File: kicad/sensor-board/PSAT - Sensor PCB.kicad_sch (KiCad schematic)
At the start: 42 parts, among them J1 533980471, J2 533980471, J3 533980471, J4 533980471, Q1 2N2222A, U1 ESP32-CAM, U2 CD-PA1616D, U3 BME280, U4 BMI323

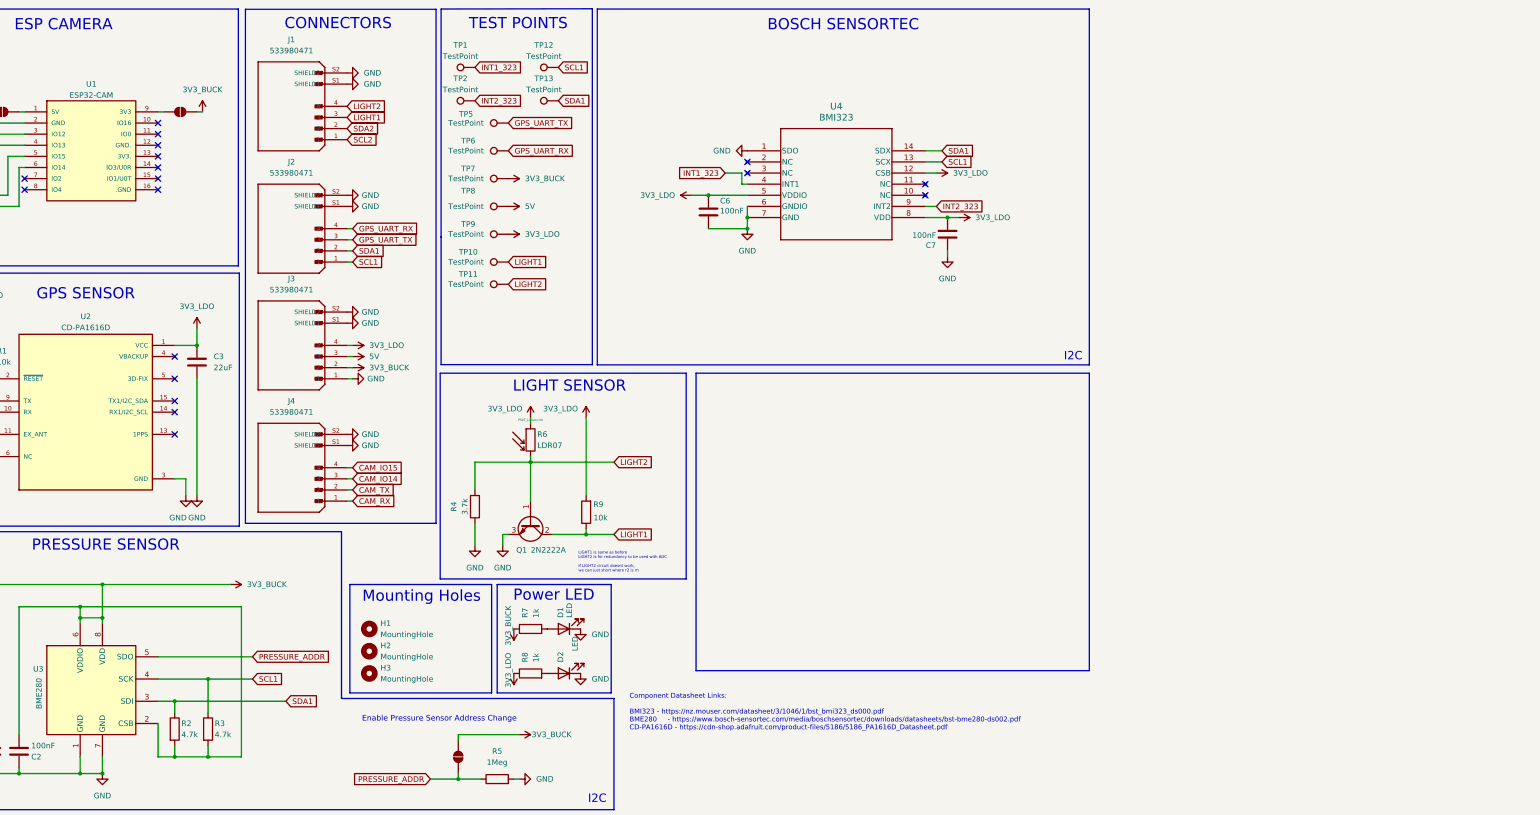
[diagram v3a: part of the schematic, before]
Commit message: feat: sensor board pcb wiring, silkscreen incomplete
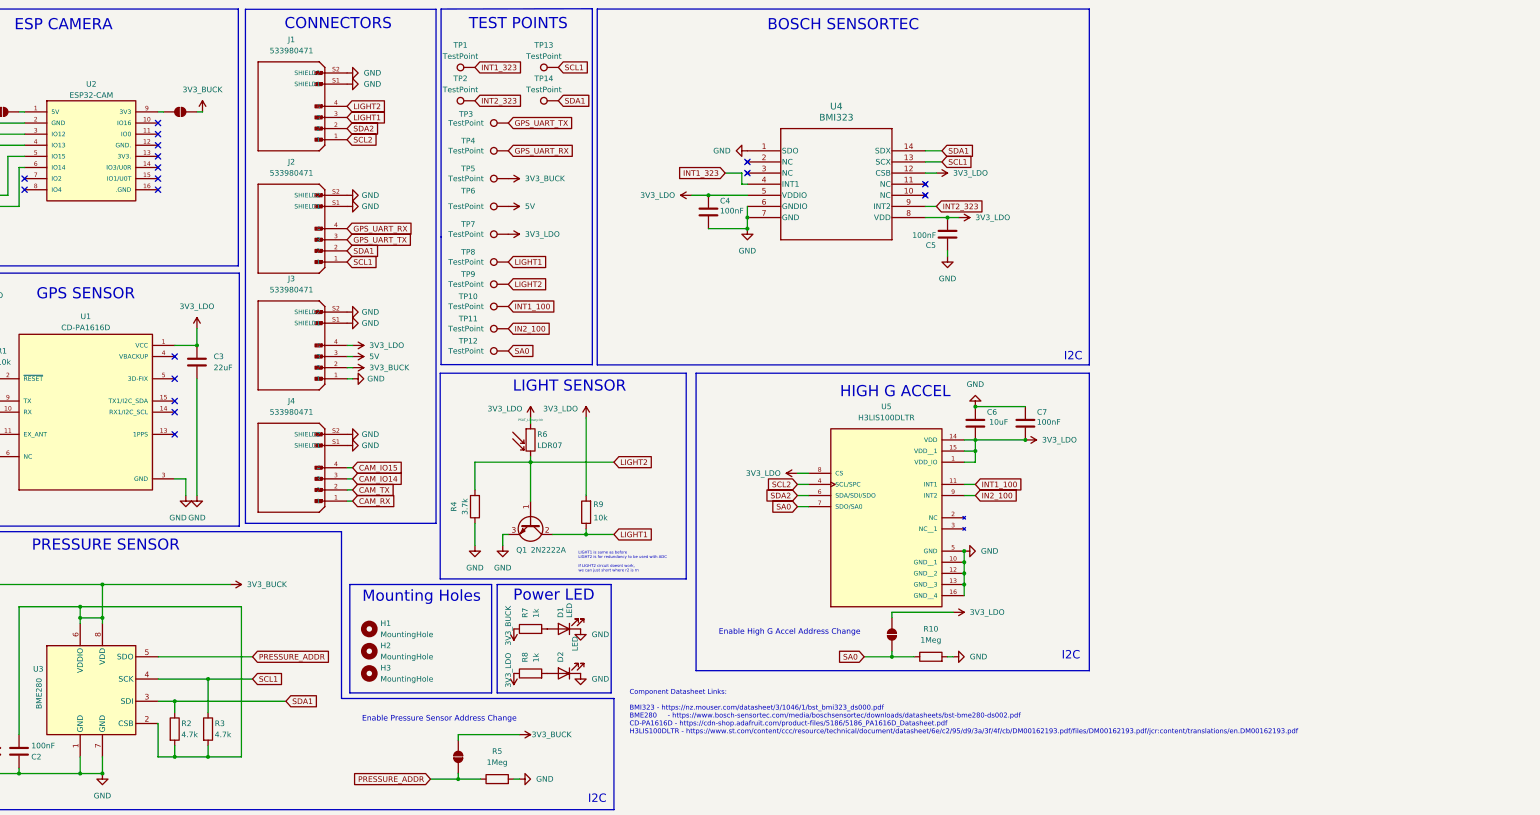
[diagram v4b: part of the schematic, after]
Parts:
- added C6: 10uF, Capacitor_SMD:C_0805_2012Metric_Pad1.18x1.45mm_HandSolder, symbol Device:C
- added C7: 100nF, Capacitor_SMD:C_0805_2012Metric_Pad1.18x1.45mm_HandSolder, symbol Device:C
- added JP4: EN_5, Jumper:SolderJumper-2_P1.3mm_Open_Pad1.0x1.5mm, symbol Jumper:SolderJumper_2_Open
- added R10: 1Meg, Resistor_SMD:R_0805_2012Metric_Pad1.20x1.40mm_HandSolder, symbol Device:R
- added TP10, TP11, TP12: TestPoint, TestPoint:TestPoint_Pad_D1.0mm, symbol Connector:TestPoint
- added U5: H3LIS100DLTR, PSAT_Library:PQFN50P300X300X100-16N, symbol H3LIS100DLTR:H3LIS100DLTR
- renumbered C6 to C4, C7 to C5, TP12 to TP13, TP13 to TP14, TP5 to TP3, TP6 to TP4, TP7 to TP5, TP8 to TP6, TP9 to TP7, TP10 to TP8, TP11 to TP9, U2 to U1, U1 to U2
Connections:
- net 3V3_LDO: now also C6.1, C7.1, JP4.1 (A), U5.1 (VDD_IO), U5.14 (VDD), U5.15 (VDD__1), U5.8 (CS)
- net GND: now also C6.2, C7.2, R10.2, U5.10 (GND__1), U5.12 (GND__2), U5.13 (GND__3), U5.16 (GND__4), U5.5 (GND)
- net SCL2: now also U5.4 (SCL/SPC)
- net SDA2: now also U5.6 (SDA/SDI/SDO)
- new net IN2_100: TP11.1, U5.9 (INT2)
- new net INT1_100: TP10.1, U5.11 (INT1)
- new net SA0: JP4.2 (B), R10.1, TP12.1, U5.7 (SDO/SA0)
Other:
- note added: "Component Datasheet Links: BMI323 - https://nz.mouser.com/datasheet/3/1046/1/bst_bmi323_ds000.pdf BME280 - https://www.bosch-sensortec.com/media/boschsensortec/downloads/datasheets/bst-bme280-ds002.pdf CD-PA1616D - https://cdn-shop.adafruit.com/product-files/5186/5186_PA1616D_Datasheet.pdf H3LIS100DLTR - https://www.st.com/content/ccc/resource/technical/document/datasheet/6e/c2/95/d9/3a/3f/4f/cb/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"
- note added: "Enable High G Accel Address Change"
- note added: "HIGH G ACCEL"
- note removed: "Component Datasheet Links: BMI323 - https://nz.mouser.com/datasheet/3/1046/1/bst_bmi323_ds000.pdf BME280 - https://www.bosch-sensortec.com/media/boschsensortec/downloads/datasheets/bst-bme280-ds002.pdf CD-PA1616D - https://cdn-shop.adafruit.com/product-files/5186/5186_PA1616D_Datasheet.pdf"

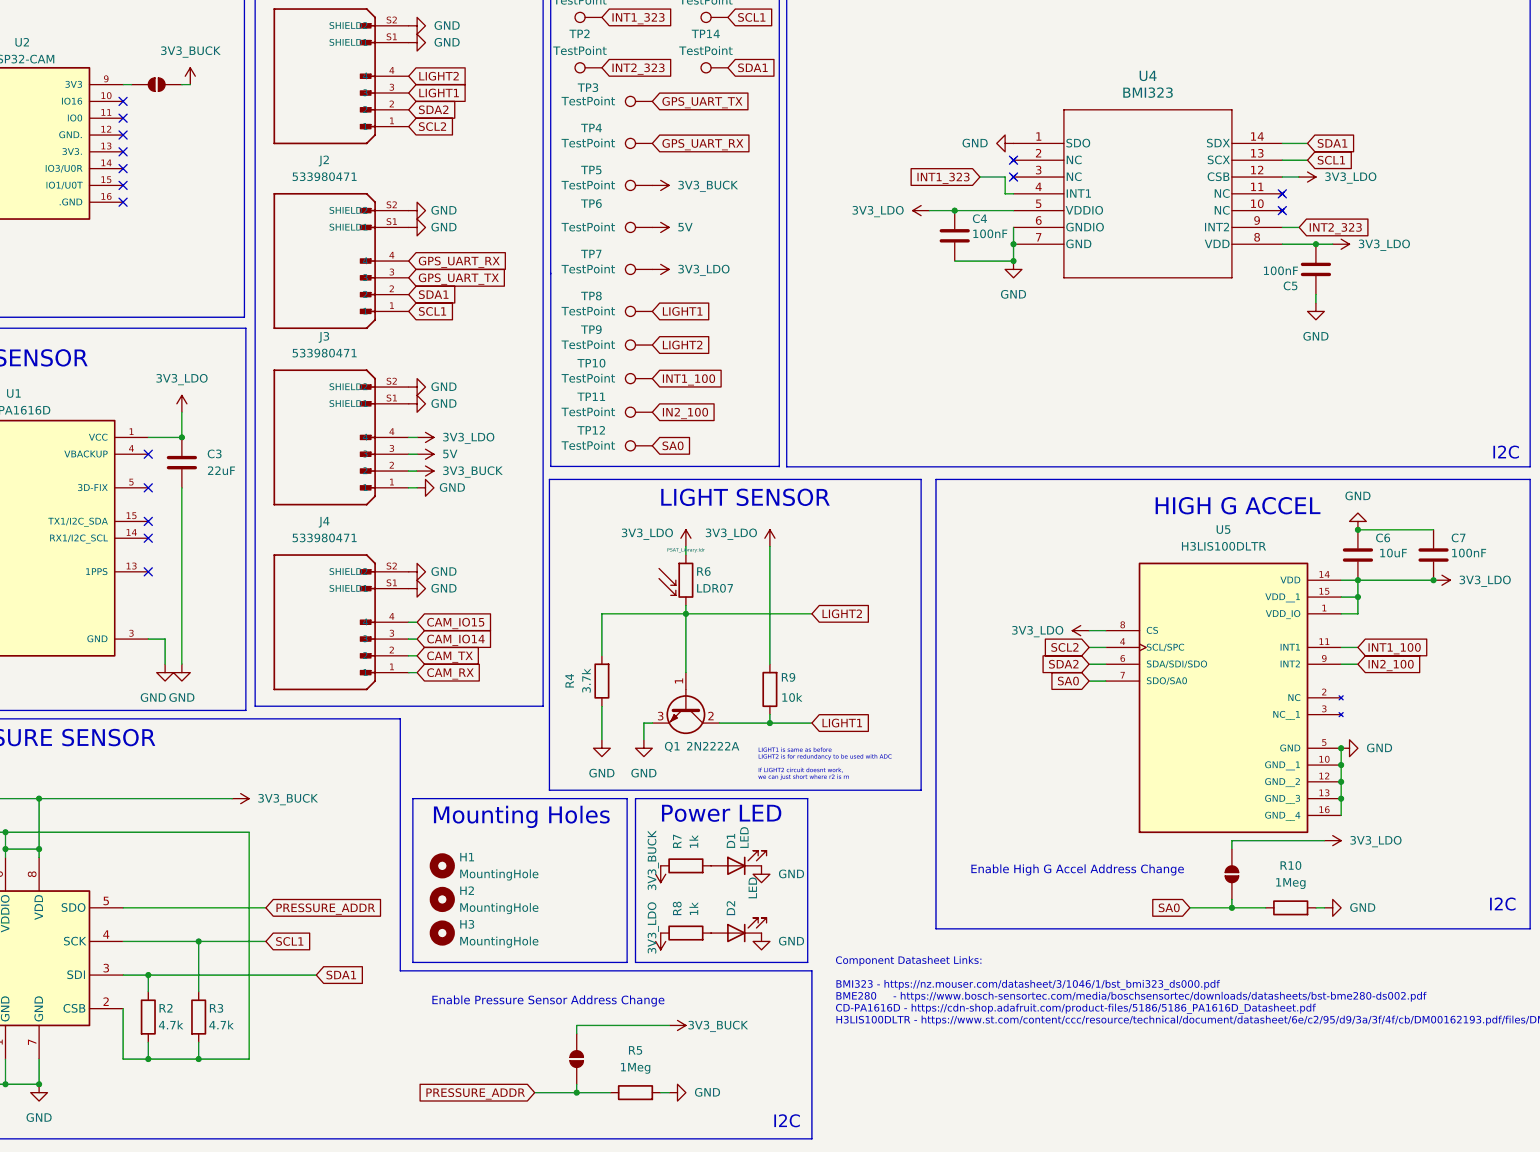
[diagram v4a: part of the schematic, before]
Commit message: feat: added improvements and removed irrelevant components
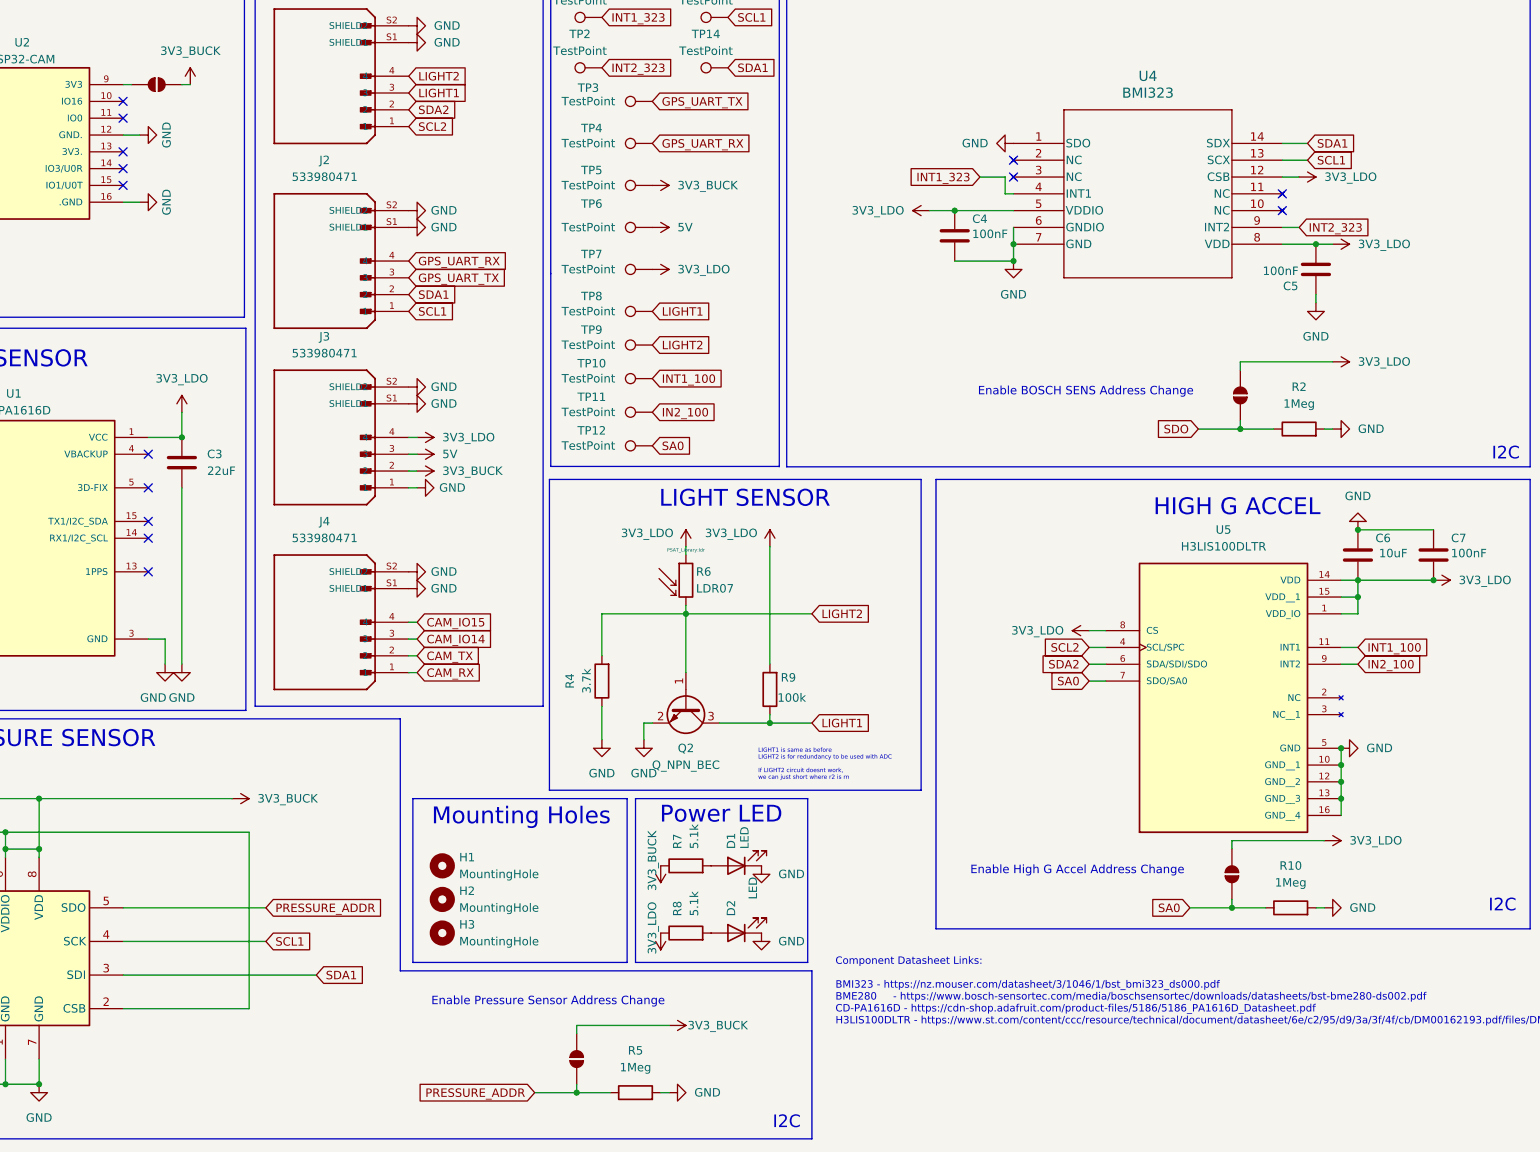
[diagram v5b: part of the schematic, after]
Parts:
- removed Q1: 2N2222A, Package_TO_SOT_SMD:SOT-23-3, symbol Transistor_BJT:Q_NPN_BCE
- removed R3: 4.7k, Resistor_SMD:R_0805_2012Metric_Pad1.20x1.40mm_HandSolder, symbol Device:R
- added JP5: EN_5, Jumper:SolderJumper-2_P1.3mm_Open_Pad1.0x1.5mm, symbol Jumper:SolderJumper_2_Open
- added Q2: Q_NPN_BEC, Package_TO_SOT_SMD:SOT-23, symbol Transistor_BJT:Q_NPN_BEC
- R2: value 4.7k -> 1Meg
- R7, R8: value 1k -> 5.1k
- R9: value 10k -> 100k
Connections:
- net 3V3_BUCK: no longer R2.2
- net 3V3_LDO: now also JP5.1 (A)
- net GND: now also R2.2, U2.12 (GND.), U2.16 (.GND), Q2.2 (E)
- net LIGHT1: now also Q2.3 (C)
- net LIGHT2: now also Q2.1 (B)
- net SDA1: no longer R2.1
- new net SDO: JP5.2 (B), R2.1
- no-connect marks 20 -> 18
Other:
- note added: "Enable BOSCH SENS Address Change"
